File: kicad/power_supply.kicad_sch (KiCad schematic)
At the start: 29 parts, among them Q1 CSD19537Q3, Q2 BSS138, U1 TPS26632RGE, U10 LMR33630ADDA, U11 LMR33630ADDA, U4 TPS82130

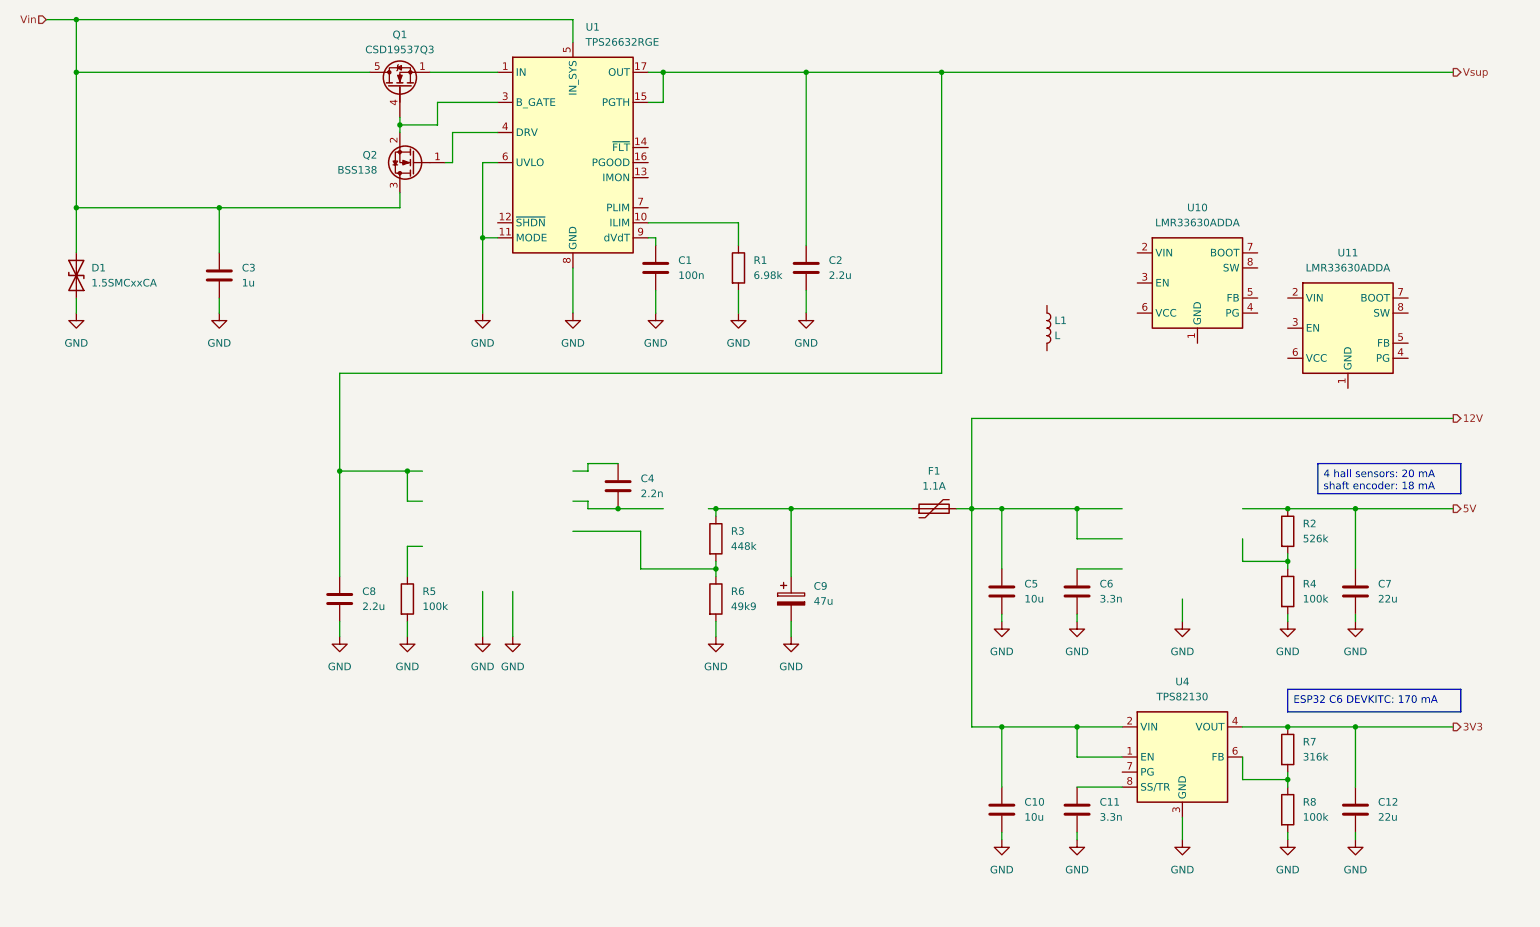
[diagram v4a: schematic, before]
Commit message: Finished the schematic and started the PCB.
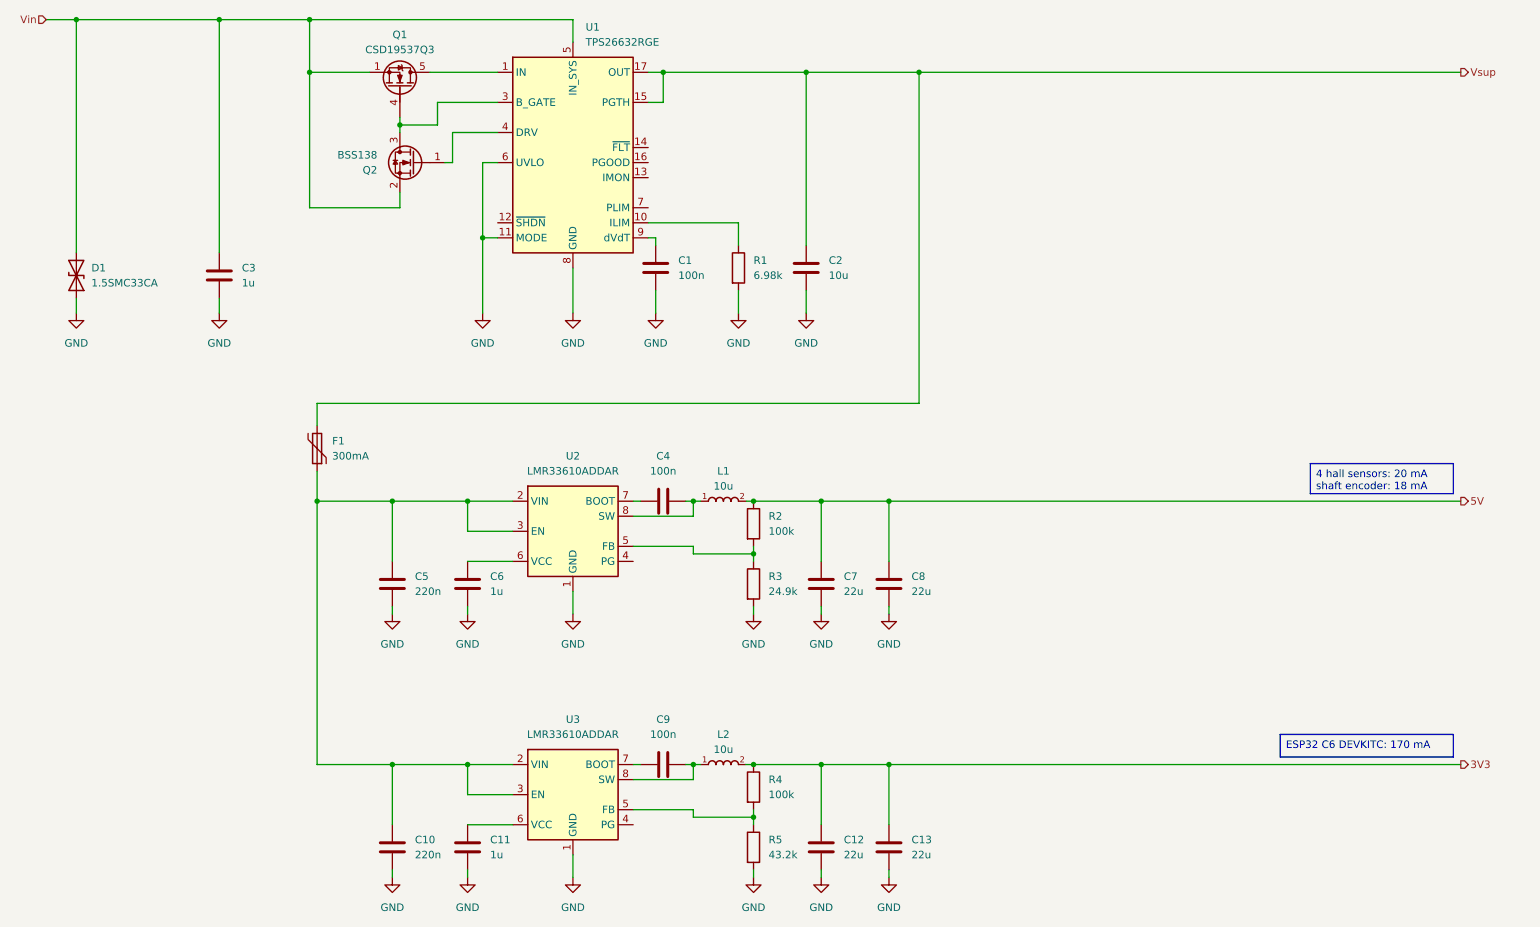
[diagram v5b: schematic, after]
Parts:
- removed C2: 2.2u, Capacitor_SMD:C_1206_3216Metric, symbol Device:C
- removed C9: 47u, Capacitor_SMD:C_Elec_6.3x5.8, symbol Device:C_Polarized
- removed L1: L, symbol Device:L
- removed R3: 448k, Resistor_SMD:R_0603_1608Metric, symbol Device:R
- removed R5: 100k, Resistor_SMD:R_0603_1608Metric, symbol Device:R
- removed R6: 49k9, Resistor_SMD:R_0603_1608Metric, symbol Device:R
- removed U10, U11: LMR33630ADDA, Package_SO:Texas_HSOP-8-1EP_3.9x4.9mm_P1.27mm_ThermalVias, symbol Regulator_Switching:LMR33630ADDA
- removed U4: TPS82130, local_library:Texas_SIL0008D_MicroSiP-8-1EP_2.8x3mm_P0.65mm_EP1.1x1.9mm_ThermalVias, symbol Regulator_Switching:TPS82130
- added C13: 22u, Capacitor_SMD:C_1206_3216Metric, symbol Device:C
- added C5: 220n, Capacitor_SMD:C_0603_1608Metric, symbol Device:C
- added C9: 100n, Capacitor_SMD:C_0603_1608Metric, symbol Device:C
- added L1, L2: 10u, local_library:IND_SRP4020TA-100M, symbol local_library:SRP4020TA-100M
- added U2, U3: LMR33610ADDAR, local_library:Texas_HSOP-8-1EP_3.9x4.9mm_P1.27mm_ThermalVias, symbol Regulator_Switching:LMR33610ADDAR
- C10: value 10u -> 220n; footprint Capacitor_SMD:C_0805_2012Metric -> Capacitor_SMD:C_0603_1608Metric; Dielectric X5R -> X7R; MP GRM21BR61E106KA73K -> GRM188R71H224KAC4J; SupplierPN 490-16824-1-ND -> 490-GRM188R71H224KAC4JCT-ND; Voltage 25V -> 50V
- C11, C6: value 3.3n -> 1u; Dielectric X7R -> X7S; MP GRM188R72A332KA01D -> GRM188C71C105KA12J; SupplierPN 490-1481-1-ND -> 490-GRM188C71C105KA12JCT-ND; Voltage 100V -> 16V
- C12, C7: footprint Capacitor_SMD:C_Elec_6.3x5.8 -> Capacitor_SMD:C_1206_3216Metric; MF Kemet -> Murata; MP A766EB226M1DLAE060 -> GRM31CC71C226ME11L; SupplierPN 399-A766EB226M1DLAE060CT-ND -> 490-17691-1-ND; Voltage 20V -> 16V
- C2: renamed from C5; MP GRM21BR61E106KA73K -> GRM21BR61H106KE43L; SupplierPN 490-16824-1-ND -> 490-18663-1-ND; Voltage 25V -> 50V
- C3: footprint Capacitor_SMD:C_0805_2012Metric -> Capacitor_SMD:C_0603_1608Metric; Dielectric X7S -> X7T; MP GRM21BC72A105KE01L -> GRM188D71H105KE01J; SupplierPN 490-14464-1-ND -> 490-GRM188D71H105KE01JCT-ND; Voltage 100V -> 50V
- C4: value 2.2n -> 100n; MP GRM188R72A222KA01D -> GRM188R72A104KA35D; SupplierPN 490-1478-1-ND -> 490-3285-1-ND
- C8: value 2.2u -> 22u; Dielectric X8L -> Polymer; MP GRM31CL8EL225KE07L -> GRM31CC71C226ME11L; SupplierPN 490-GRM31CL8EL225KE07LCT-ND -> 490-17691-1-ND; Voltage 100V -> 16V
- D1: value 1.5SMCxxCA -> 1.5SMC33CA; Voltage 58V -> 33V
- F1: value 1.1A -> 300mA; footprint local_library:Fuse_2920_7451Metric -> Fuse:Fuse_1812_4532Metric; MF Littelfuse -> Bourns; MP 2920L110/60MR -> MF-MSMF030-2; SupplierPN 18-2920L110/60MR-ACT-ND -> MF-MSMF030-2CT-ND
- R2: value 526k -> 100k
- R3: renamed from R4; value 100k -> 24.9k; MF YAGEO -> Yageo; MP RC0603FR-07100KL -> RC0603FR-0724K9L; SupplierPN 311-100KHRCT-ND -> 311-24.9KHRCT-ND
- R4: renamed from R8; MF YAGEO -> Yageo
- R5: renamed from R7; value 316k -> 43.2k; MP RC0603FR-07100KL -> RC0603FR-0743K2L; SupplierPN 311-100KHRCT-ND -> 311-43.2KHRCT-ND
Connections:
- net 3V3: now also R4.1, C13.1, L2.2; no longer R5.1
- net 5V: now also C8.1, L1.2
- net GND: now also R5.2, C13.2, C5.2, U2.1 (GND), U2.9 (GND), U3.1 (GND), U3.9 (GND); no longer R4.2
- net Vin: now also Q1.1 (S), Q1.2 (S), Q1.3 (S), Q2.2 (S); no longer Q1.5 (D), Q2.3 (D)
- net Vsup: now also C2.1, F1.2; no longer C8.1
- net at F1.1: now also C10.1, C5.1, U2.2 (VIN), U2.3 (EN), U3.2 (VIN), U3.3 (EN)
- net at C11.1: now also U3.6 (VCC)
- net at Q1.4 (G), U1.3 (B_GATE): now also Q2.3 (D); no longer Q2.2 (S)
- net at C4.1: now also U2.7 (BOOT)
- net at C4.2: now also L1.1, U2.8 (SW)
- net at R2.2, R3.1: now also U2.5 (FB)
- net at C6.1: now also U2.6 (VCC)
- removed net 12V: C10.1, C2.1, F1.2
- new net: Q1.5 (D), U1.1 (IN), U1.2 (IN)
- new net: R4.2, R5.1, U3.5 (FB)
- new net: C9.1, U3.7 (BOOT)
- new net: C9.2, L2.1, U3.8 (SW)
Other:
- moved on the sheet: C2, C7, F1, Q1, Q2, R2, R3, R4, R5

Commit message: Completed the PCB design. Ready for final review.
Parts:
- D1: value 1.5SMC33CA -> SMBJ33CA; footprint Diode_SMD:D_SMC -> Diode_SMD:D_SMB; MF Diotec Semiconductor -> Bourns; MP 1.5SMCJ58CA -> SMBJ33CA; SupplierPN 4878-1.5SMCJ58CACT-ND -> SMBJ33CABCT-ND
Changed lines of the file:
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@@
 	(title_block
 		(title "TV slider")
-		(date "2025-10-06")
-		(rev "1")
+		(date "2025-12-23")
+		(rev "1.0")
 		(company "NX Solutions")
 	)
@@
 			)
 		)
-		(property "Value" "1.5SMC33CA"
+		(property "Value" "SMBJ33CA"
 			(at 34.29 60.9599 90)
 			(effects
@@
 			)
 		)
-		(property "Footprint" "Diode_SMD:D_SMC"
+		(property "Footprint" "Diode_SMD:D_SMB"
 			(at 36.83 59.69 0)
 			(effects
@@
 			)
 		)
-		(property "Datasheet" "https://www.vishay.com/docs/88303/15smc.pdf"
+		(property "Datasheet" ""
 			(at 31.75 59.69 0)
 			(effects
@@
 			)
 		)
-		(property "Description" "1500W bidirectional TVS diode, SMC (DO-201AB)"
+		(property "Description" ""
 			(at 31.75 59.69 0)
 			(effects
@@
 			)
 		)
-		(property "SupplierPN" "4878-1.5SMCJ58CACT-ND"
+		(property "SupplierPN" "SMBJ33CABCT-ND"
 			(at 31.75 59.69 90)
 			(effects
@@
 			)
 		)
-		(property "MF" "Diotec Semiconductor"
+		(property "MF" "Bourns"
 			(at 31.75 59.69 90)
 			(effects
@@
 			)
 		)
-		(property "MP" "1.5SMCJ58CA"
+		(property "MP" "SMBJ33CA"
 			(at 31.75 59.69 90)
 			(effects

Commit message: Reviewed the part numbers, footprints and pin numbers.
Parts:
- C11, C6: Dielectric X7S -> X7T; MP GRM188C71C105KA12J -> GRM188D71H105KE01J; SupplierPN 490-GRM188C71C105KA12JCT-ND -> 490-GRM188D71H105KE01JCT-ND; Voltage 16V -> 50V
- C12, C13, C7, C8: Dielectric Polymer -> X7S
- L1, L2: MF (none) -> Bourns; MP (none) -> SRP4020TA-100M; Supplier (none) -> Digi-Key; SupplierPN (none) -> SRP4020TA-100MCT-ND
- R1: MP RC0603FR-07100KL -> RC0603FR-076K98L; SupplierPN 311-100KHRCT-ND -> 311-6.98KHRCT-ND
- U2, U3: MF (none) -> Texas Instruments; MP (none) -> LMR33610ADDAR; Supplier (none) -> Digi-Key; SupplierPN (none) -> 296-LMR33610ADDARCT-ND

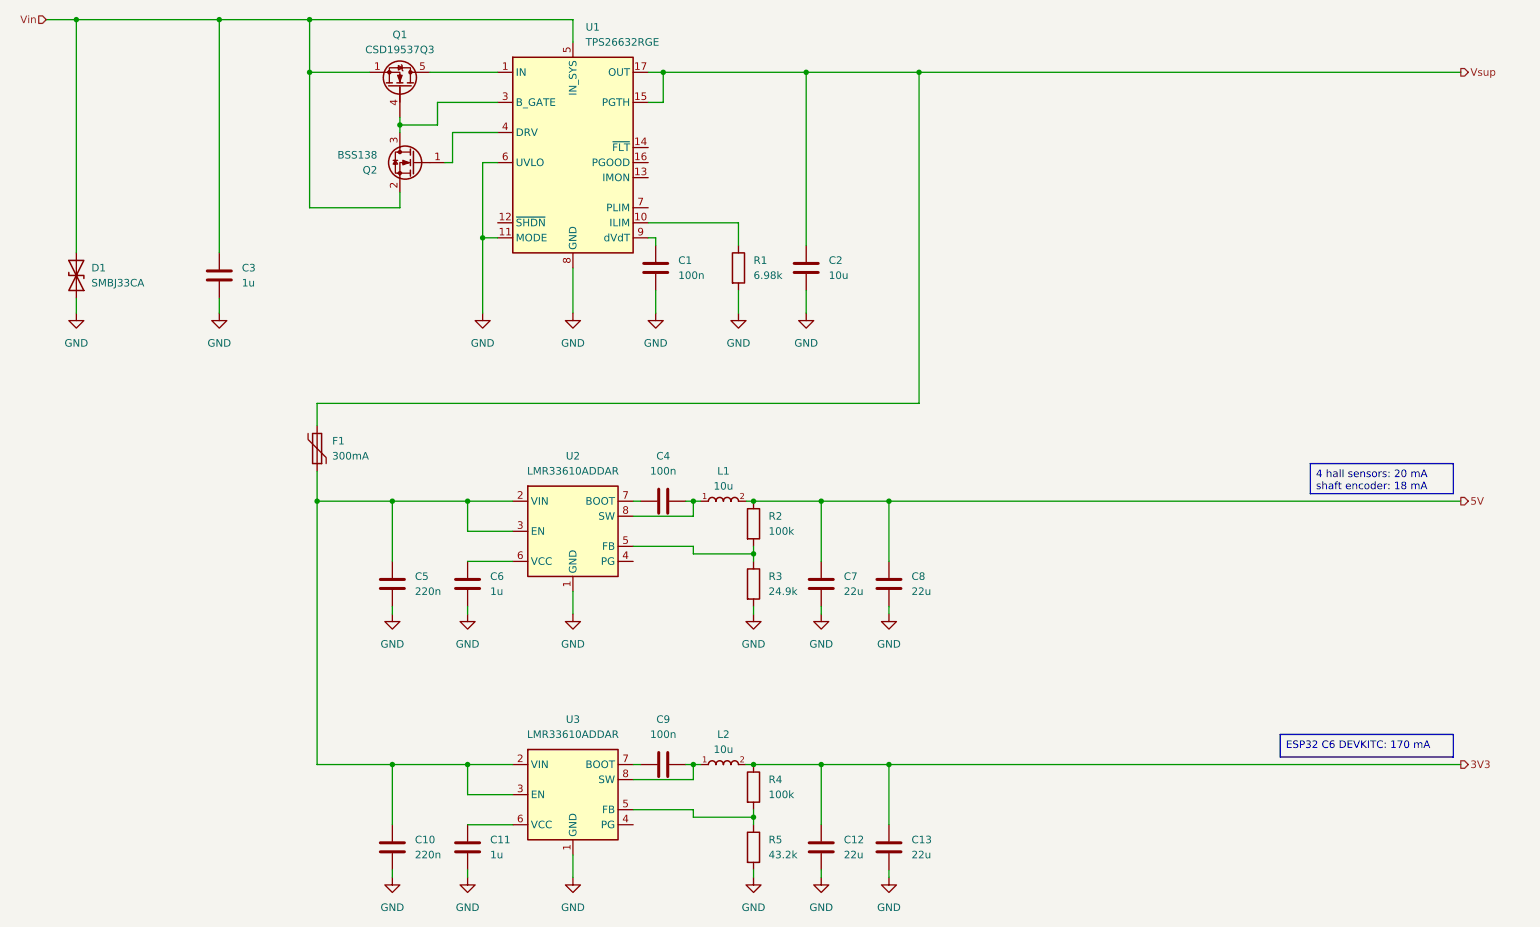
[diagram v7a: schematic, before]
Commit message: Re-annotated and added extra capacitors for the 5V and 3V3 DC-DC converters. Added testpoints to the electronic fuse.
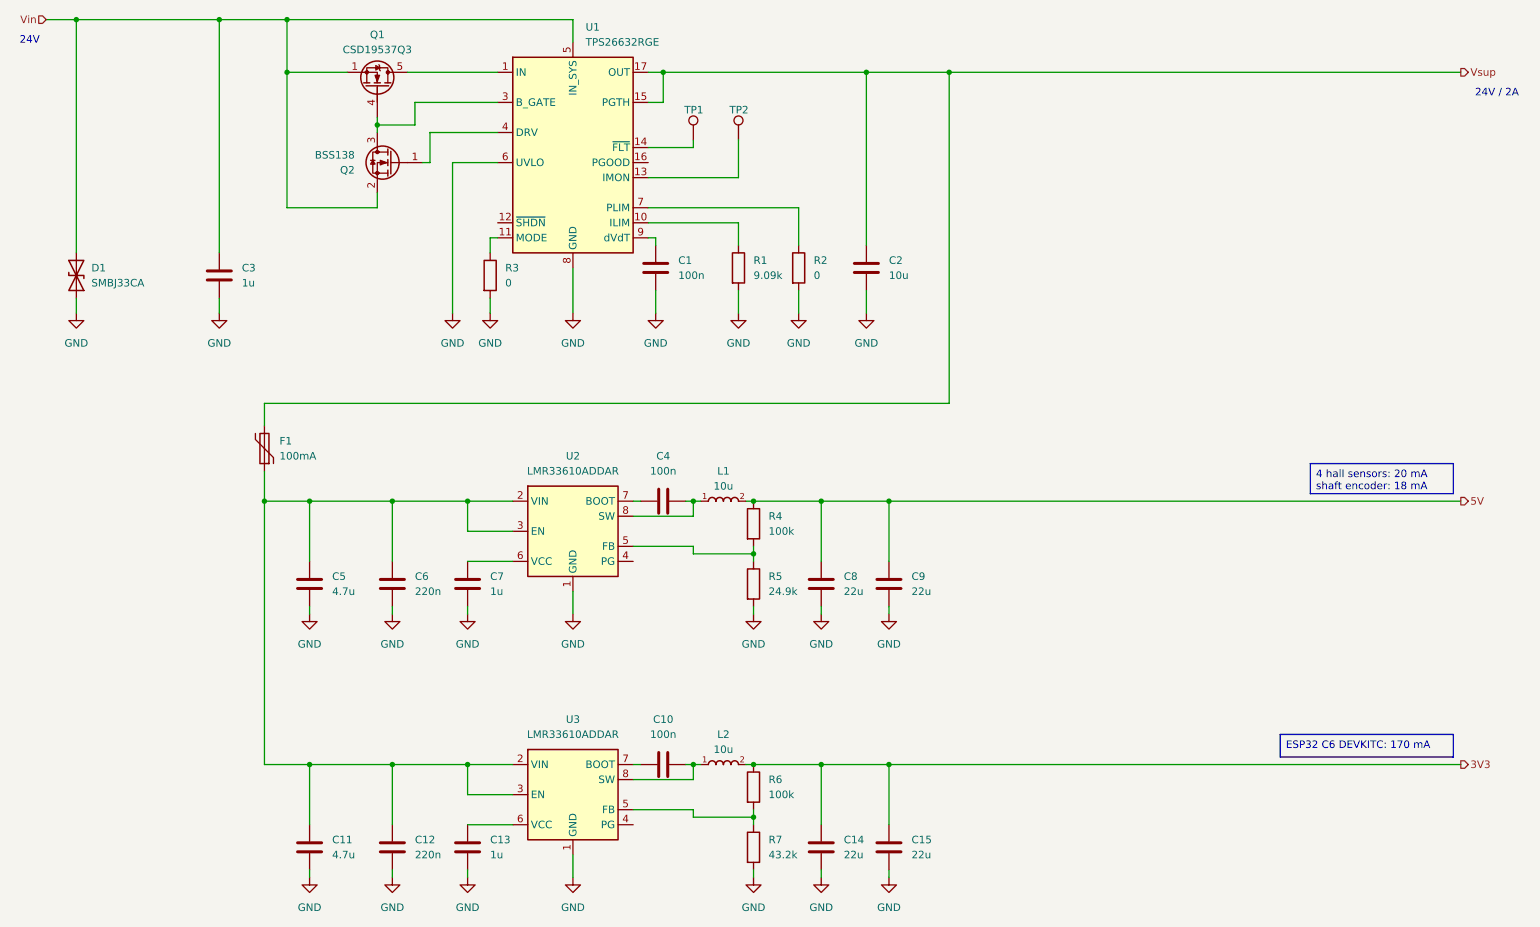
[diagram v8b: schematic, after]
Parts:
- added C11, C5: 4.7u, Capacitor_SMD:C_0805_2012Metric, symbol Device:C
- added R2, R3: 0, Resistor_SMD:R_0603_1608Metric, symbol Device:R
- added TP1: ~{FLT}, TestPoint:TestPoint_Pad_D1.0mm, symbol Connector:TestPoint
- added TP2: IMON, TestPoint:TestPoint_Pad_D1.0mm, symbol Connector:TestPoint
- F1: value 300mA -> 100mA; MP MF-MSMF030-2 -> MF-MSMF010-2; SupplierPN MF-MSMF030-2CT-ND -> MF-MSMF010-2CT-ND
- R1: value 6.98k -> 9.09k; MP RC0603FR-076K98L -> RC0603FR-079K09L; SupplierPN 311-6.98KHRCT-ND -> 311-9.09KHRCT-ND
- renumbered C9 to C10, C10 to C12, C11 to C13, C12 to C14, C13 to C15, C5 to C6, C6 to C7, C7 to C8, C8 to C9, R2 to R4, R3 to R5, R4 to R6, R5 to R7
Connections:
- net GND: now also C11.2, C5.2, R2.2, R3.2; no longer U1.11 (MODE)
- net at C12.1, C6.1, F1.1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: now also C11.1, C5.1
- net at U1.13 (IMON): now also TP2.1
- net at U1.14 (~{FLT}): now also TP1.1
- net at U1.7 (PLIM): now also R2.1
- new net: R3.1, U1.11 (MODE)
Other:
- note added: "24V"
- note added: "24V / 2A"
- moved on the sheet: C2, F1, Q1, Q2
